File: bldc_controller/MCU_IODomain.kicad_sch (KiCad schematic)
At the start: 7 parts, among them U5 STM32G474RET3

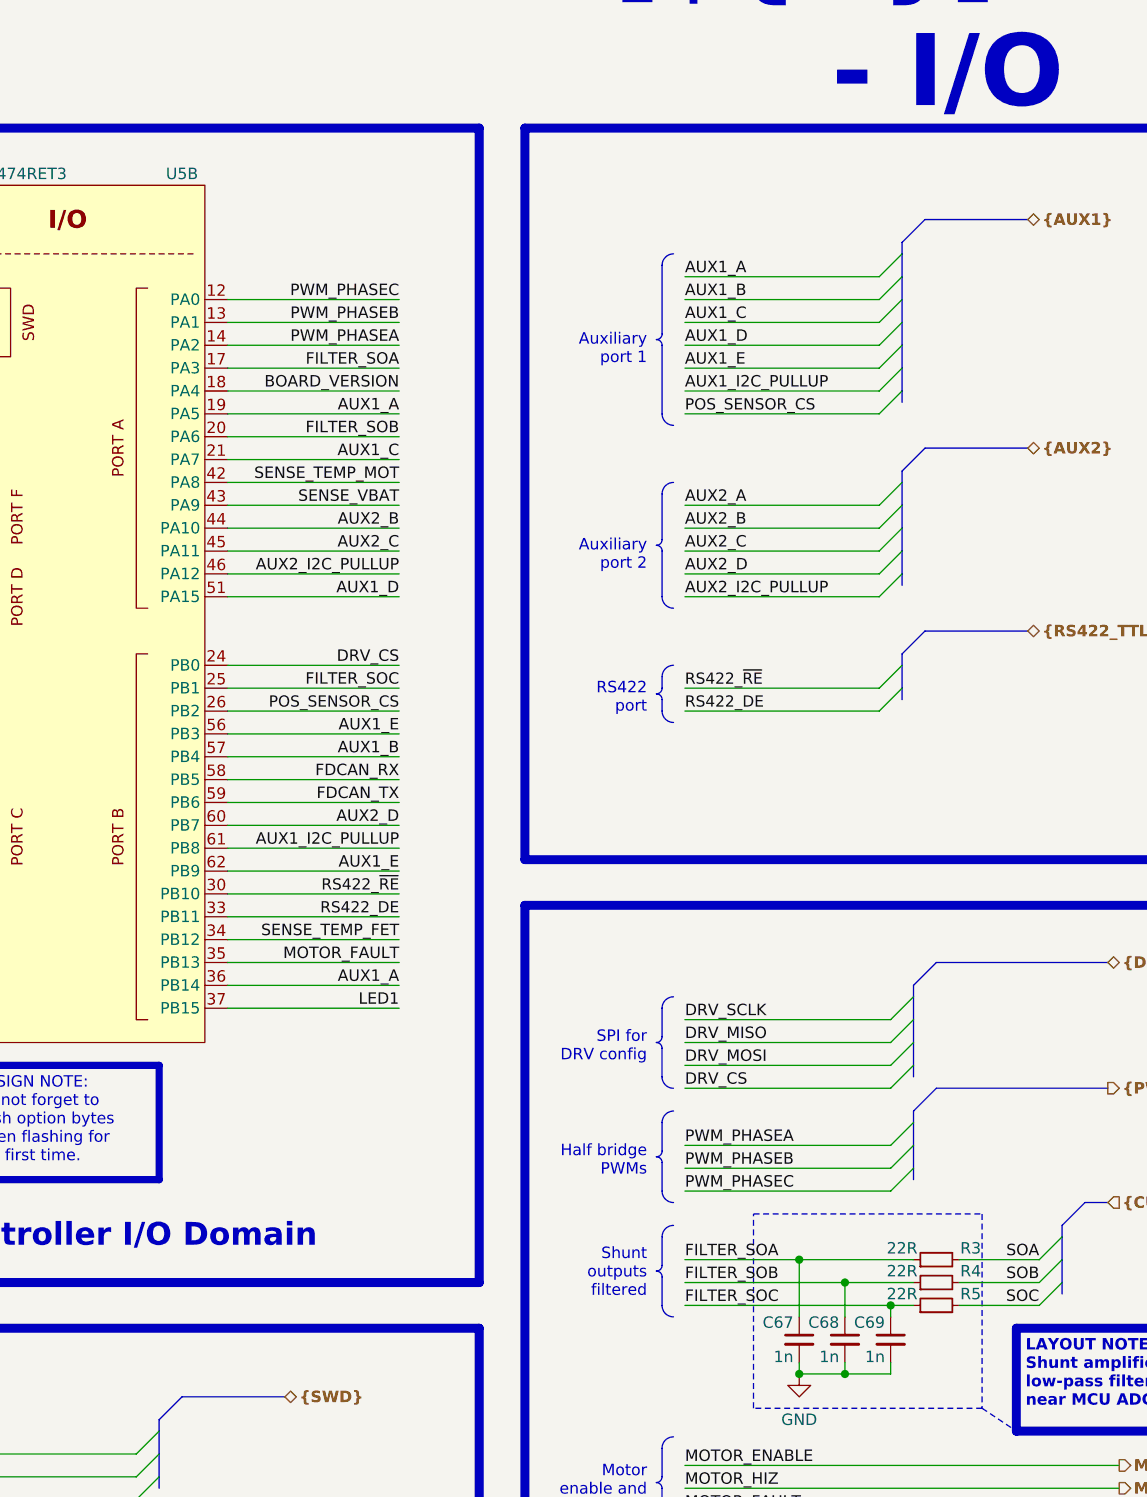
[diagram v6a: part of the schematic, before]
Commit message: routed all signals. TODO: redo all power polygons and ensure good return paths/reference. Added 3d models
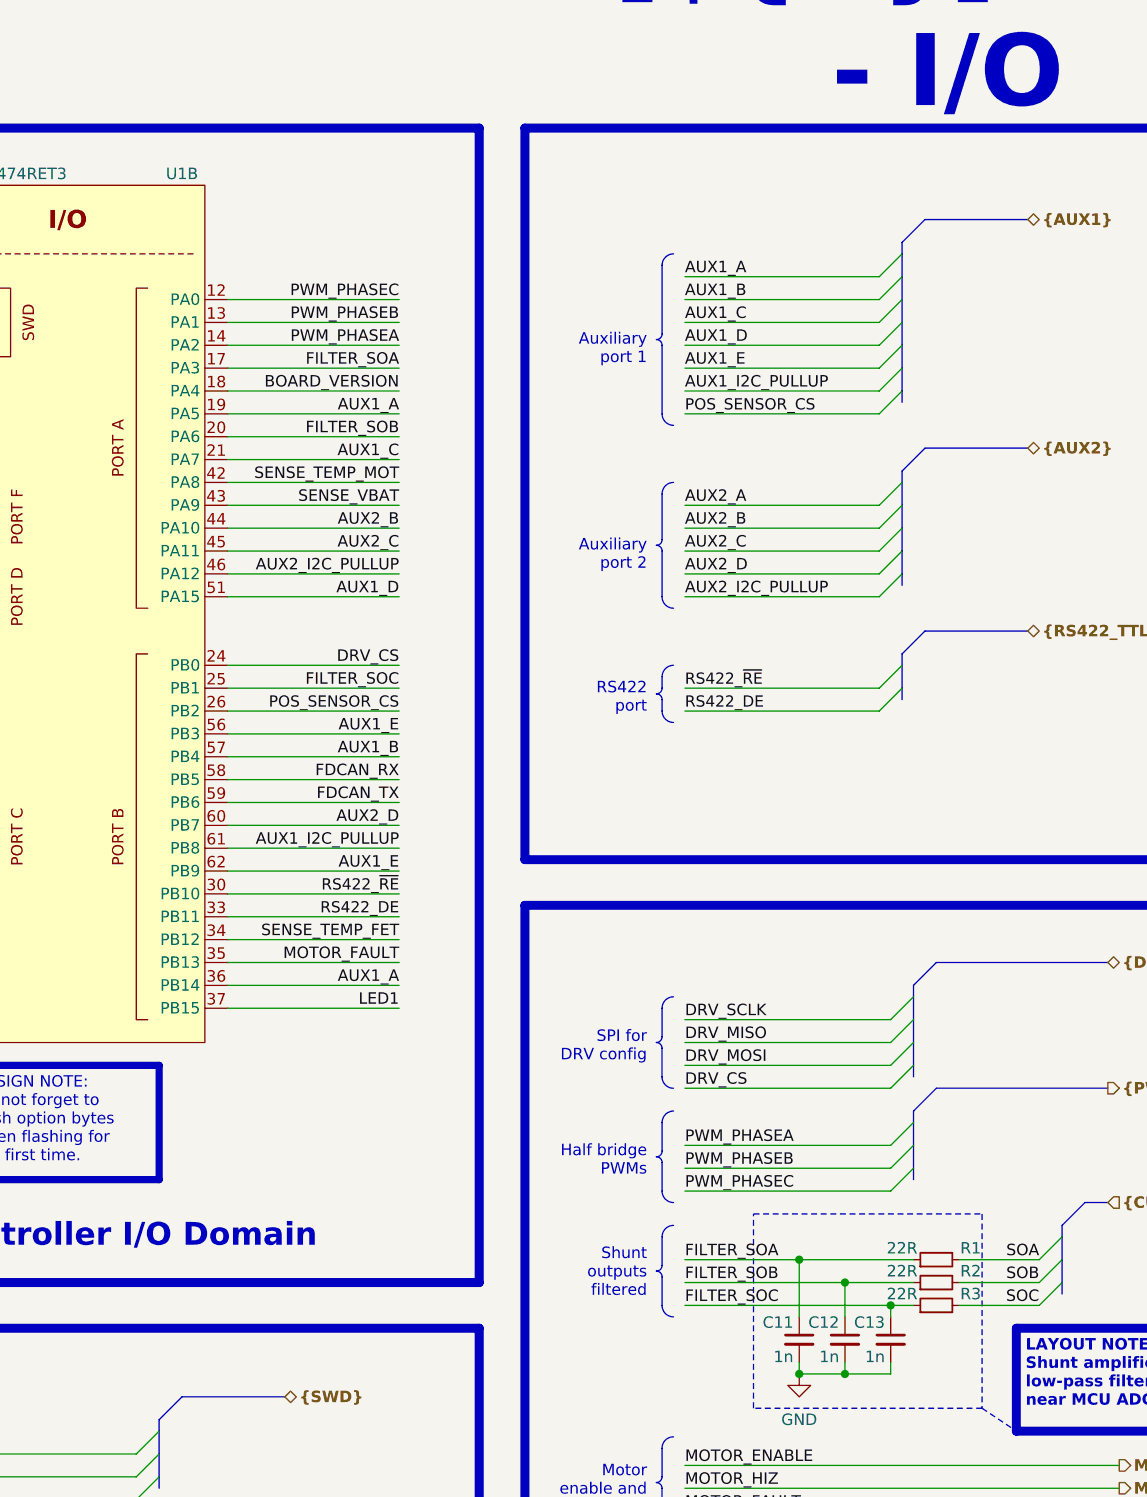
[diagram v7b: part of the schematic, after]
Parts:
- renumbered C67 to C11, C68 to C12, C69 to C13, R3 to R1, R4 to R2, R5 to R3, U5 to U1
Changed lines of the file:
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@@
   (symbol (lib_id "power:GND") (at 193.04 177.8 0) (unit 1)
     (in_bom yes) (on_board yes) (dnp no)
-    (property "Reference" "#PWR065" (at 193.04 184.15 0)
+    (property "Reference" "#PWR016" (at 193.04 184.15 0)
       (effects (font (size 1.27 1.27)) hide)
     )
@@
       (project "bldc_controller"
         (path "/0650c7a8-acba-429c-9f8e-eec0baf0bc1c/fede4c36-00cc-4d3d-b71c-5243ba232202/e6015f1e-cbce-46f4-85e1-3d5463a17dc1"
-          (reference "#PWR065") (unit 1)
+          (reference "#PWR016") (unit 1)
         )
       )
@@
   (symbol (lib_id "Device:C_Small") (at 193.04 173.99 0) (mirror y) (unit 1)
     (in_bom yes) (on_board yes) (dnp no)
-    (property "Reference" "C67" (at 192.405 172.085 0)
+    (property "Reference" "C11" (at 192.405 172.085 0)
       (effects (font (size 1.27 1.27)) (justify left))
     )
@@
       (project "bldc_controller"
         (path "/0650c7a8-acba-429c-9f8e-eec0baf0bc1c/fede4c36-00cc-4d3d-b71c-5243ba232202/e6015f1e-cbce-46f4-85e1-3d5463a17dc1"
-          (reference "C67") (unit 1)
+          (reference "C11") (unit 1)
         )
       )
@@
   (symbol (lib_id "Device:R_Small") (at 208.28 165.1 90) (unit 1)
     (in_bom yes) (on_board yes) (dnp no)
-    (property "Reference" "R3" (at 212.09 163.83 90)
+    (property "Reference" "R1" (at 212.09 163.83 90)
       (effects (font (size 1.27 1.27)))
     )
@@
       (project "bldc_controller"
         (path "/0650c7a8-acba-429c-9f8e-eec0baf0bc1c/fede4c36-00cc-4d3d-b71c-5243ba232202/e6015f1e-cbce-46f4-85e1-3d5463a17dc1"
-          (reference "R3") (unit 1)
+          (reference "R1") (unit 1)
         )
       )
@@
   (symbol (lib_id "Device:C_Small") (at 198.12 173.99 0) (mirror y) (unit 1)
     (in_bom yes) (on_board yes) (dnp no)
-    (property "Reference" "C68" (at 197.485 172.085 0)
+    (property "Reference" "C12" (at 197.485 172.085 0)
       (effects (font (size 1.27 1.27)) (justify left))
     )
@@
       (project "bldc_controller"
         (path "/0650c7a8-acba-429c-9f8e-eec0baf0bc1c/fede4c36-00cc-4d3d-b71c-5243ba232202/e6015f1e-cbce-46f4-85e1-3d5463a17dc1"
-          (reference "C68") (unit 1)
+          (reference "C12") (unit 1)
         )
       )
@@
   (symbol (lib_id "Device:R_Small") (at 208.28 167.64 90) (unit 1)
     (in_bom yes) (on_board yes) (dnp no)
-    (property "Reference" "R4" (at 212.09 166.37 90)
+    (property "Reference" "R2" (at 212.09 166.37 90)
       (effects (font (size 1.27 1.27)))
     )
@@
       (project "bldc_controller"
         (path "/0650c7a8-acba-429c-9f8e-eec0baf0bc1c/fede4c36-00cc-4d3d-b71c-5243ba232202/e6015f1e-cbce-46f4-85e1-3d5463a17dc1"
-          (reference "R4") (unit 1)
+          (reference "R2") (unit 1)
         )
       )
@@
   (symbol (lib_id "Device:C_Small") (at 203.2 173.99 0) (mirror y) (unit 1)
     (in_bom yes) (on_board yes) (dnp no)
-    (property "Reference" "C69" (at 202.565 172.085 0)
+    (property "Reference" "C13" (at 202.565 172.085 0)
       (effects (font (size 1.27 1.27)) (justify left))
     )
@@
       (project "bldc_controller"
         (path "/0650c7a8-acba-429c-9f8e-eec0baf0bc1c/fede4c36-00cc-4d3d-b71c-5243ba232202/e6015f1e-cbce-46f4-85e1-3d5463a17dc1"
-          (reference "C69") (unit 1)
+          (reference "C13") (unit 1)
         )
       )
@@
   (symbol (lib_id "0_mcu:STM32G474RETx") (at 111.76 91.44 0) (unit 2)
     (in_bom yes) (on_board yes) (dnp no)
-    (property "Reference" "U5" (at 124.46 44.45 0)
+    (property "Reference" "U1" (at 124.46 44.45 0)
       (effects (font (size 1.27 1.27)))
     )
@@
       (project "bldc_controller"
         (path "/0650c7a8-acba-429c-9f8e-eec0baf0bc1c/fede4c36-00cc-4d3d-b71c-5243ba232202/e6015f1e-cbce-46f4-85e1-3d5463a17dc1"
-          (reference "U5") (unit 2)
+          (reference "U1") (unit 2)
         )
       )
@@
   (symbol (lib_id "Device:R_Small") (at 208.28 170.18 90) (unit 1)
     (in_bom yes) (on_board yes) (dnp no)
-    (property "Reference" "R5" (at 212.09 168.91 90)
+    (property "Reference" "R3" (at 212.09 168.91 90)
       (effects (font (size 1.27 1.27)))
     )
@@
       (project "bldc_controller"
         (path "/0650c7a8-acba-429c-9f8e-eec0baf0bc1c/fede4c36-00cc-4d3d-b71c-5243ba232202/e6015f1e-cbce-46f4-85e1-3d5463a17dc1"
-          (reference "R5") (unit 1)
-        )
-      )
+          (reference "R3") (unit 1)
+        )
+      )
